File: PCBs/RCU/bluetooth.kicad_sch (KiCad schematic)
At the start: 31 parts, among them J400 USB_C_Receptacle_USB2.0, Q400 Q_NMOS_DGS, Q401 Q_NMOS_DGS, Q402 Q_PMOS_DGS, Q403 Q_NMOS_DGS, SW400 SW_Push, U400 CH340C, U401 DG2788ADN-T1-GE4, U402 ESP32-MINI-1

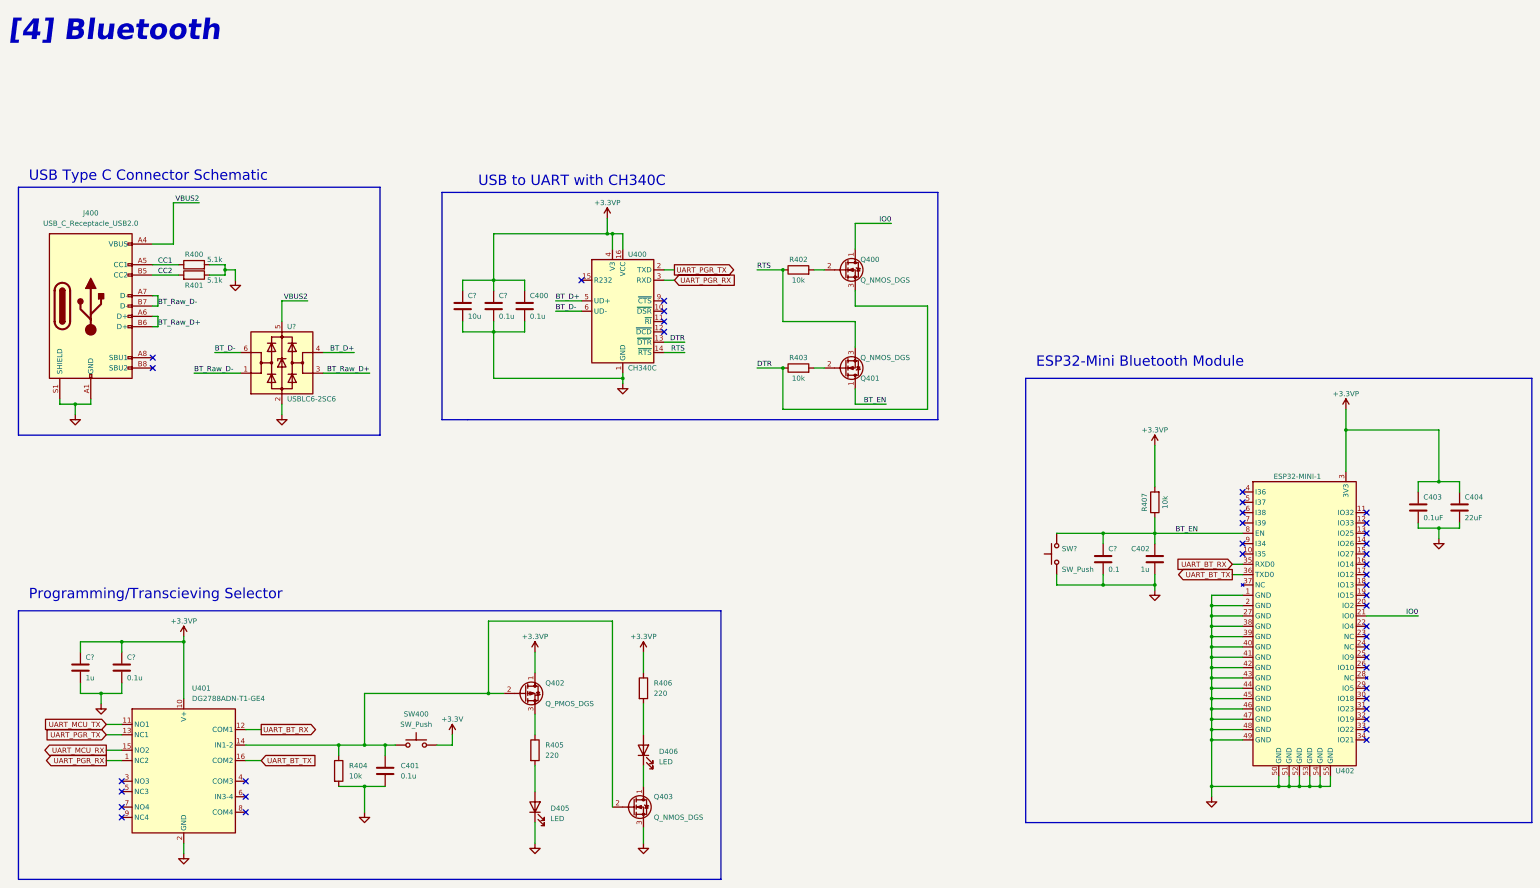
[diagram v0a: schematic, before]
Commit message: Fully annotated Bluetooth schematic
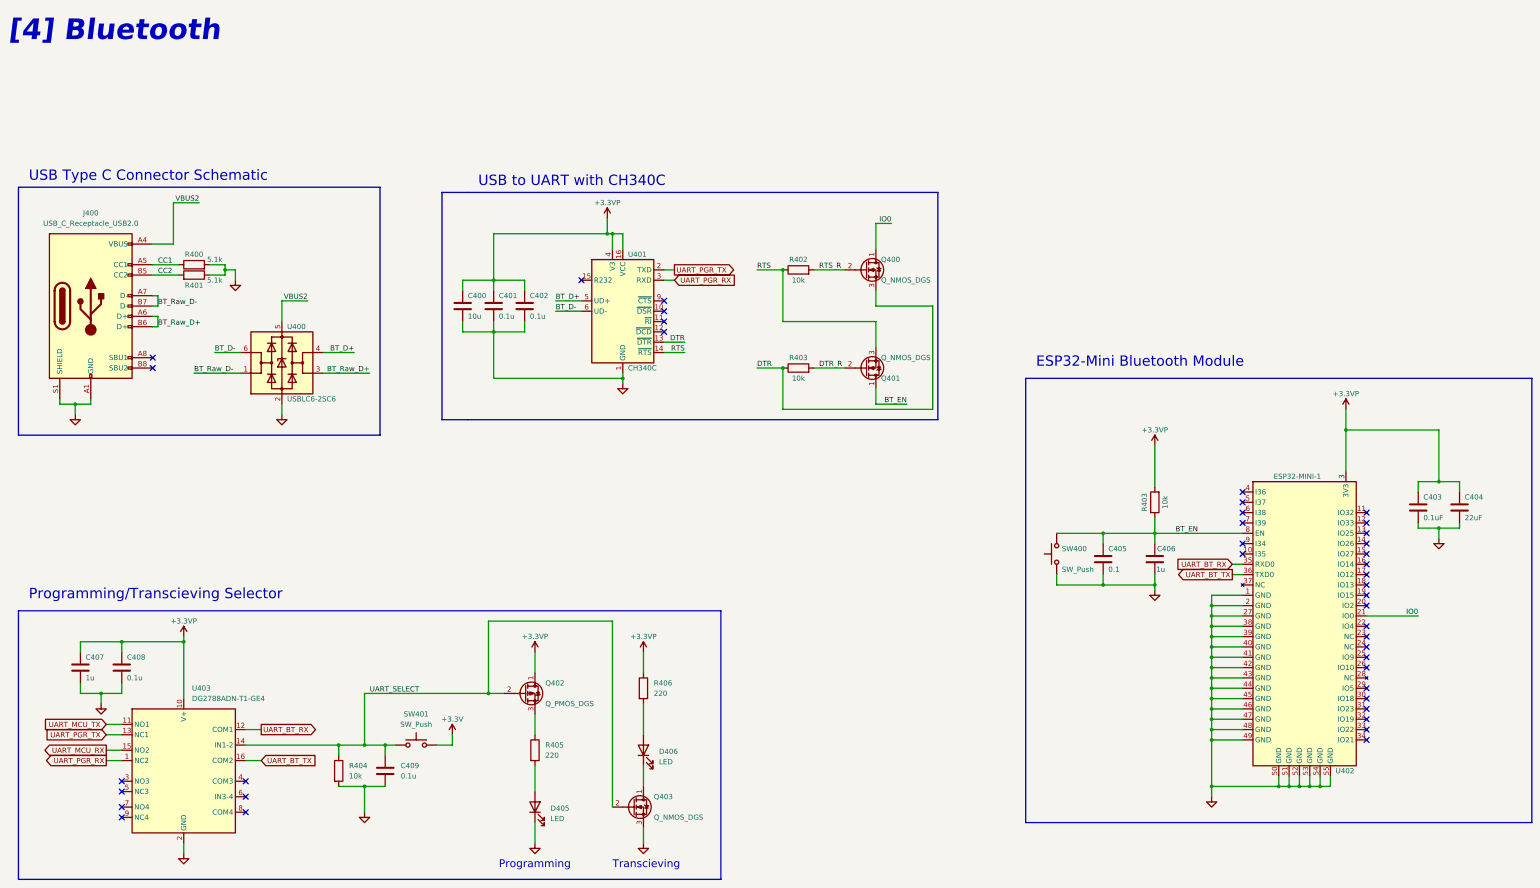
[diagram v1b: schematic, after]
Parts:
- gave numbers to parts that had none: 7
- renumbered C400 to C402, C402 to C406, C401 to C409, R407 to R403, SW400 to SW401, U400 to U401, U401 to U403
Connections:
- net UART_SELECT: now reaches C409.1, Q402.2 (G), Q403.2 (G), R404.1, SW401.1, U403.14 (IN1-2)
- net DTR_R: now reaches Q401.2 (G), R403.2
- net RTS_R: now reaches Q400.2 (G), R402.2
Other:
- note added: "Programming"
- note added: "Transcieving"
- moved on the sheet: Q400, Q401

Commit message: Schematic cleanup
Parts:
- C400: value 10u -> (none)
- C401, C402, C409: value 0.1u -> (none)
- C405: value 0.1 -> (none)
- C406: value 1u -> (none)
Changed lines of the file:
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@@
       (effects (font (size 1.27 1.27)) (justify left))
     )
-    (property "Value" "0.1u" (id 1) (at 160.02 100.33 0)
+    (property "Value" "" (id 1) (at 160.02 100.33 0)
       (effects (font (size 1.27 1.27)) (justify left))
     )
@@
       (effects (font (size 1.27 1.27)) (justify left))
     )
-    (property "Value" "0.1u" (id 1) (at 128.27 213.3599 0)
+    (property "Value" "" (id 1) (at 128.27 213.3599 0)
       (effects (font (size 1.27 1.27)) (justify left))
     )
@@
       (effects (font (size 1.27 1.27)) (justify left))
     )
-    (property "Value" "0.1u" (id 1) (at 152.4 100.33 0)
+    (property "Value" "" (id 1) (at 152.4 100.33 0)
       (effects (font (size 1.27 1.27)) (justify left))
     )
@@
       (effects (font (size 1.27 1.27)) (justify left))
     )
-    (property "Value" "10u" (id 1) (at 144.78 100.33 0)
+    (property "Value" "" (id 1) (at 144.78 100.33 0)
       (effects (font (size 1.27 1.27)) (justify left))
     )
@@
       (effects (font (size 1.27 1.27)) (justify left))
     )
-    (property "Value" "1u" (id 1) (at 316.23 162.56 0)
+    (property "Value" "" (id 1) (at 317.5 162.56 0)
       (effects (font (size 1.27 1.27)) (justify left))
     )
@@
       (effects (font (size 1.27 1.27)) (justify left))
     )
-    (property "Value" "0.1" (id 1) (at 302.26 162.56 0)
-      (effects (font (size 1.27 1.27)) (justify left))
-    )
+    (property "Value" "" (id 1) (at 302.26 162.56 0)
+      (effects (font (size 1.27 1.27)) (justify left))
+    )

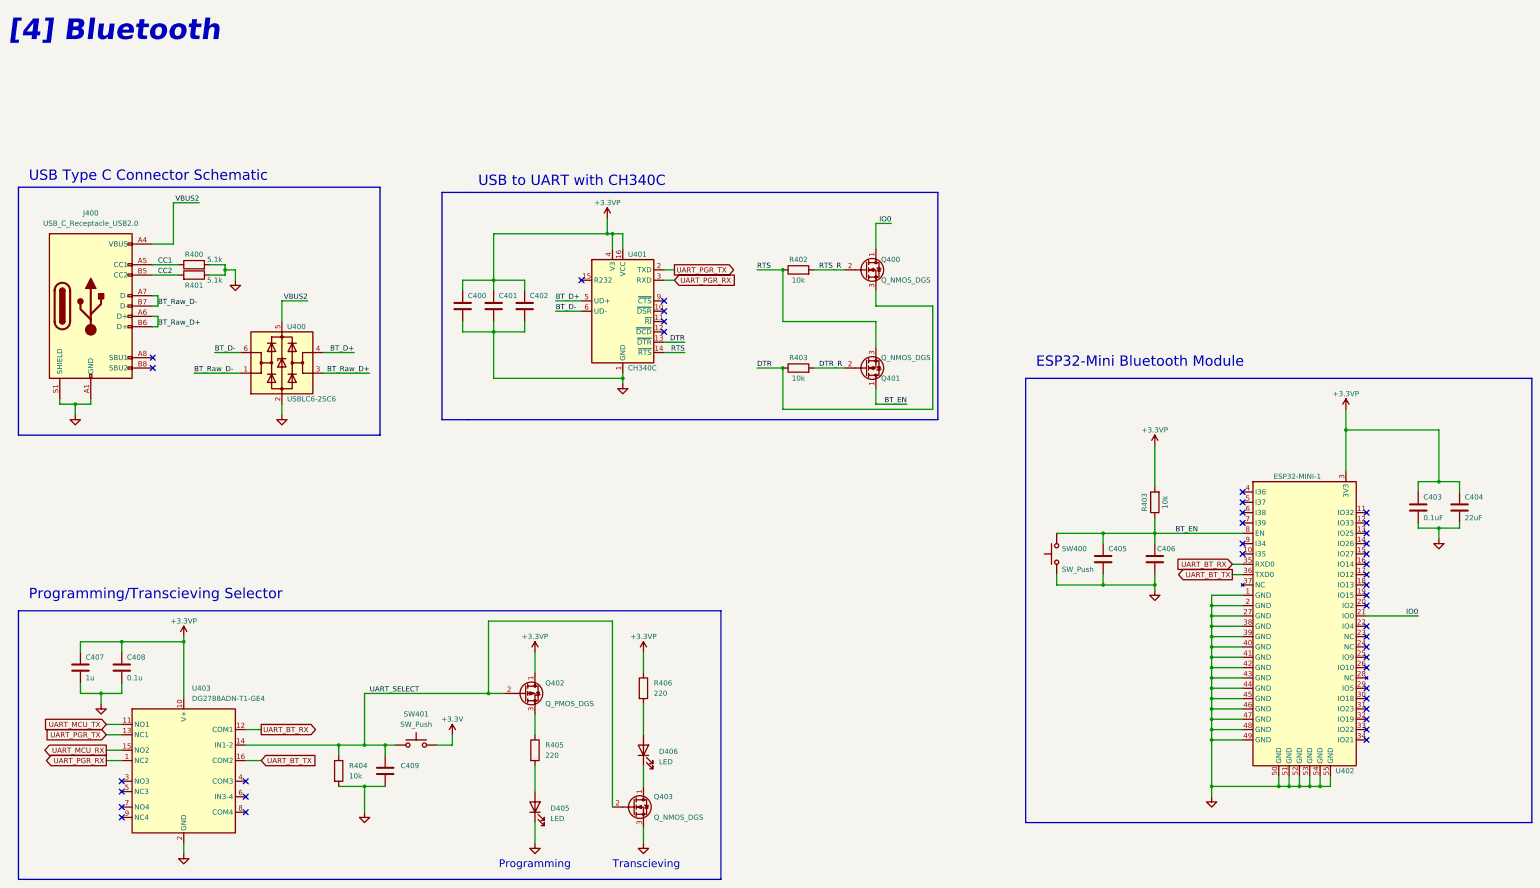
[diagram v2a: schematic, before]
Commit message: Wrote that first regulator in power schematic also powers the external memory
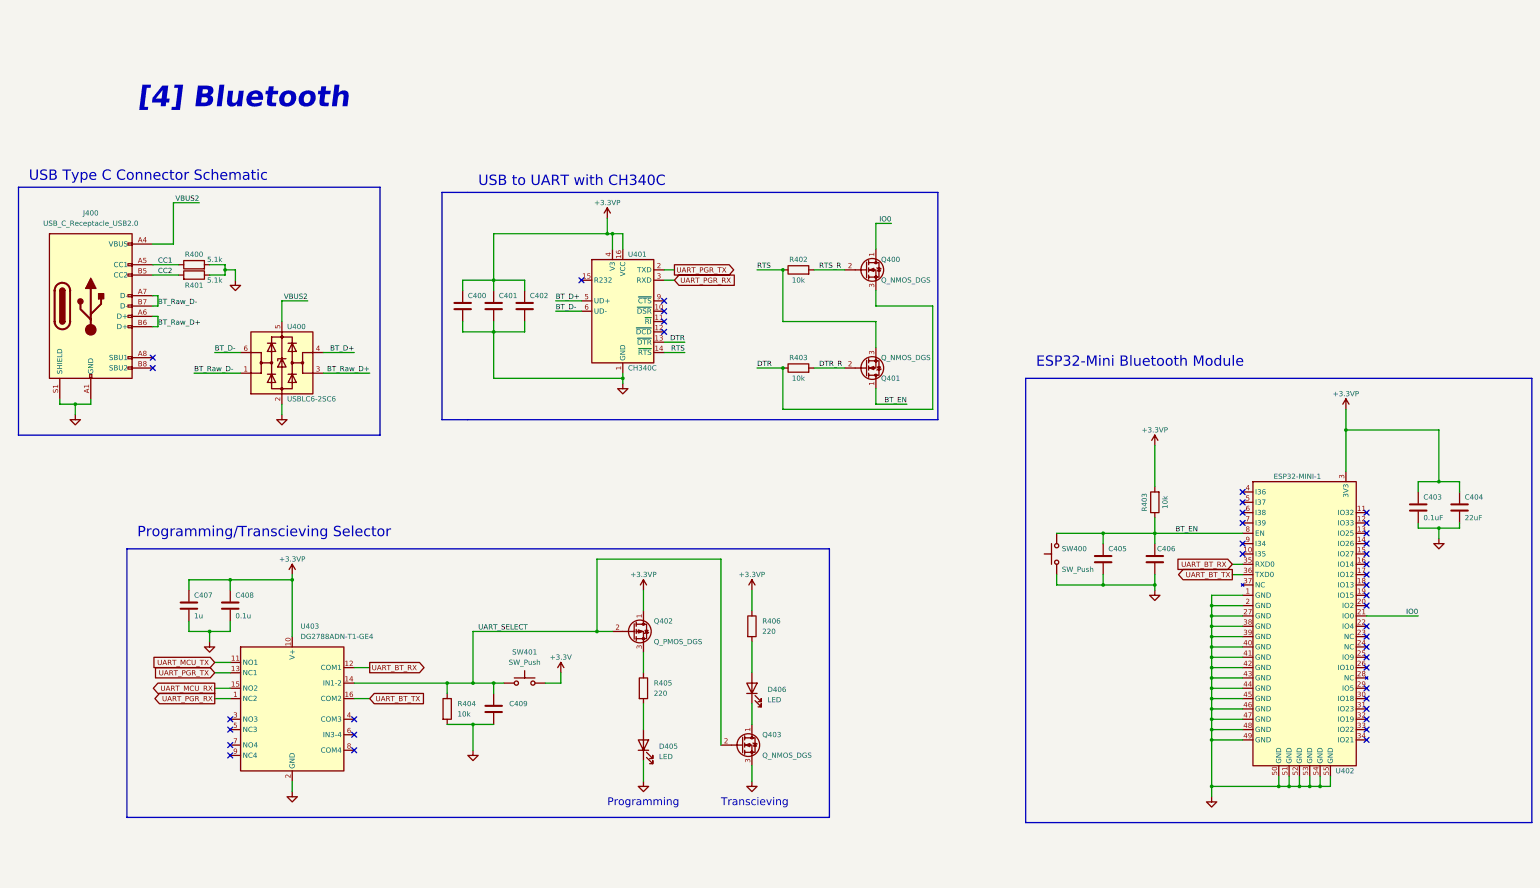
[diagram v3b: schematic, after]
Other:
- moved on the sheet: C407, C408, C409, D405, D406, Q402, Q403, R404, R405, R406, SW401, U403

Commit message: Corrected SPI_MOSI and SPI_MISO labels on U700 - external memory
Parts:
- C400: value (none) -> 10uF
- C401, C402, C405, C409: value (none) -> 0.1uF
- C406: value (none) -> 1uF
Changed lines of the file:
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@@
       (effects (font (size 1.27 1.27)) (justify left))
     )
-    (property "Value" "" (id 1) (at 160.02 100.33 0)
+    (property "Value" "0.1uF" (id 1) (at 160.02 100.33 0)
       (effects (font (size 1.27 1.27)) (justify left))
     )
@@
       (effects (font (size 1.27 1.27)) (justify left))
     )
-    (property "Value" "" (id 1) (at 154.94 198.1199 0)
+    (property "Value" "0.1uF" (id 1) (at 154.94 198.1199 0)
       (effects (font (size 1.27 1.27)) (justify left))
     )
@@
       (effects (font (size 1.27 1.27)) (justify left))
     )
-    (property "Value" "" (id 1) (at 152.4 100.33 0)
+    (property "Value" "0.1uF" (id 1) (at 152.4 100.33 0)
       (effects (font (size 1.27 1.27)) (justify left))
     )
@@
       (effects (font (size 1.27 1.27)) (justify left))
     )
-    (property "Value" "" (id 1) (at 144.78 100.33 0)
+    (property "Value" "10uF" (id 1) (at 144.78 100.33 0)
       (effects (font (size 1.27 1.27)) (justify left))
     )
@@
       (effects (font (size 1.27 1.27)) (justify left))
     )
-    (property "Value" "" (id 1) (at 317.5 162.56 0)
+    (property "Value" "1uF" (id 1) (at 317.5 162.56 0)
       (effects (font (size 1.27 1.27)) (justify left))
     )
@@
       (effects (font (size 1.27 1.27)) (justify left))
     )
-    (property "Value" "" (id 1) (at 302.26 162.56 0)
-      (effects (font (size 1.27 1.27)) (justify left))
-    )
+    (property "Value" "0.1uF" (id 1) (at 302.26 162.56 0)
+      (effects (font (size 1.27 1.27)) (justify left))
+    )

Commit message: Changed UART selector led resistor values, and assigned colours
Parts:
- D405, D406: value LED -> (none)
- R405, R406: value 220 -> (none)
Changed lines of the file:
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@@
     (effects (font (size 5.08 5.08) (thickness 1.016) bold italic) (justify left bottom))
   )
-  (text "Programming" (at 179.07 220.98 0)
+  (text "Programming" (at 205.74 220.98 0)
     (effects (font (size 1.905 1.905)) (justify left bottom))
   )
@@
     (effects (font (size 2.54 2.54)) (justify left bottom))
   )
-  (text "Transcieving\n" (at 207.01 220.98 0)
+  (text "Transcieving\n" (at 180.34 220.98 0)
     (effects (font (size 1.905 1.905)) (justify left bottom))
   )
@@
       (effects (font (size 1.27 1.27)) (justify left))
     )
-    (property "Value" "220" (id 1) (at 190.5 193.0399 0)
+    (property "Value" "" (id 1) (at 190.5 193.0399 0)
       (effects (font (size 1.27 1.27)) (justify left))
     )
@@
       (effects (font (size 1.27 1.27)) (justify right))
     )
-    (property "Value" "LED" (id 1) (at 218.44 194.6274 90)
+    (property "Value" "" (id 1) (at 218.44 194.6274 90)
       (effects (font (size 1.27 1.27)) (justify right))
     )
@@
       (effects (font (size 1.27 1.27)) (justify left))
     )
-    (property "Value" "220" (id 1) (at 217.17 177.7999 0)
+    (property "Value" "" (id 1) (at 217.17 177.7999 0)
       (effects (font (size 1.27 1.27)) (justify left))
     )
@@
       (effects (font (size 1.27 1.27)) (justify right))
     )
-    (property "Value" "LED" (id 1) (at 191.77 208.5974 90)
+    (property "Value" "" (id 1) (at 191.77 208.5974 90)
       (effects (font (size 1.27 1.27)) (justify right))
     )

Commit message: Add microcontroller, USB receptable and Connx05 footprints
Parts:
- D405: value (none) -> Green LED
- D406: value (none) -> Yellow LED
- R405: value (none) -> 40R
- R406: value (none) -> 280
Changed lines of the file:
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@@
       (effects (font (size 1.27 1.27)) (justify left))
     )
-    (property "Value" "" (id 1) (at 190.5 193.0399 0)
+    (property "Value" "40R" (id 1) (at 190.5 193.0399 0)
       (effects (font (size 1.27 1.27)) (justify left))
     )
@@
       (effects (font (size 1.27 1.27)) (justify right))
     )
-    (property "Value" "" (id 1) (at 218.44 194.6274 90)
+    (property "Value" "Yellow LED" (id 1) (at 218.44 194.6274 90)
       (effects (font (size 1.27 1.27)) (justify right))
     )
@@
       (effects (font (size 1.27 1.27)) (justify left))
     )
-    (property "Value" "" (id 1) (at 217.17 177.7999 0)
+    (property "Value" "280" (id 1) (at 217.17 177.7999 0)
       (effects (font (size 1.27 1.27)) (justify left))
     )
@@
       (effects (font (size 1.27 1.27)) (justify right))
     )
-    (property "Value" "" (id 1) (at 191.77 208.5974 90)
+    (property "Value" "Green LED" (id 1) (at 191.77 208.5974 90)
       (effects (font (size 1.27 1.27)) (justify right))
     )

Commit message: Add footprint to rest of IC's except ESP32
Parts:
- J400: footprint (none) -> Connector_USB:USB_C_Receptacle_HRO_TYPE-C-31-M-12
- U401: footprint Package_SO:SOIC-16_3.9x9.9mm_P1.27mm -> Package_SO:SOP-16_3.9x9.9mm_P1.27mm
- U403: footprint (none) -> UQFN-16(1.8x2.6):QFN40P260X180X55-16N
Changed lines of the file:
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@@
       (effects (font (size 1.27 1.27)) (justify left))
     )
-    (property "Footprint" "" (id 2) (at 82.55 175.26 0)
+    (property "Footprint" "UQFN-16(1.8x2.6):QFN40P260X180X55-16N" (id 2) (at 82.55 175.26 0)
       (effects (font (size 1.27 1.27)) hide)
     )
@@
     (property "Reference" "J400" (id 0) (at 52.07 74.93 0))
     (property "Value" "USB_C_Receptacle_USB2.0" (id 1) (at 52.07 77.47 0))
-    (property "Footprint" "" (id 2) (at 55.88 97.79 0)
+    (property "Footprint" "Connector_USB:USB_C_Receptacle_HRO_TYPE-C-31-M-12" (id 2) (at 55.88 97.79 0)
       (effects (font (size 1.27 1.27)) hide)
     )
@@
       (effects (font (size 1.27 1.27)) (justify left))
     )
-    (property "Footprint" "Package_SO:SOIC-16_3.9x9.9mm_P1.27mm" (id 2) (at 184.15 113.03 0)
+    (property "Footprint" "Package_SO:SOP-16_3.9x9.9mm_P1.27mm" (id 2) (at 184.15 113.03 0)
       (effects (font (size 1.27 1.27)) (justify left) hide)
     )

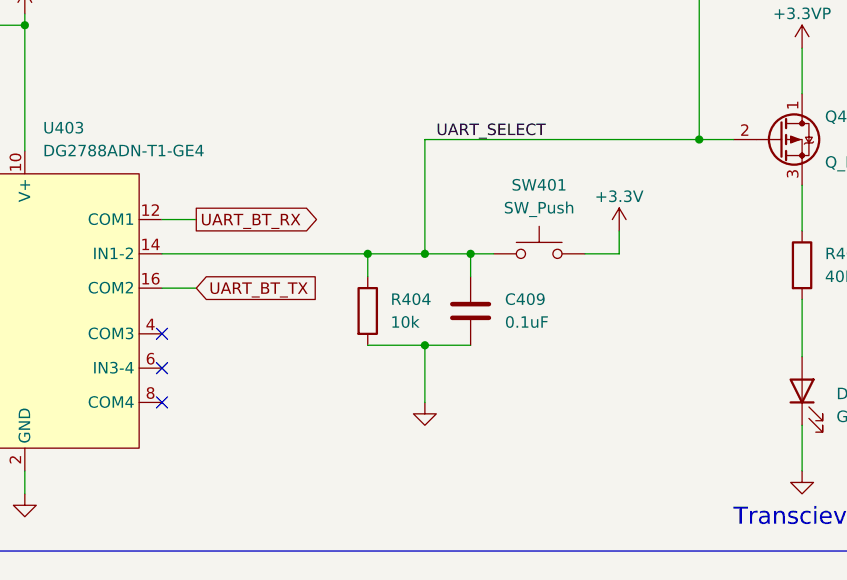
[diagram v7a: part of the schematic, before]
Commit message: Changed Programming/Transcieving button to a slide switch
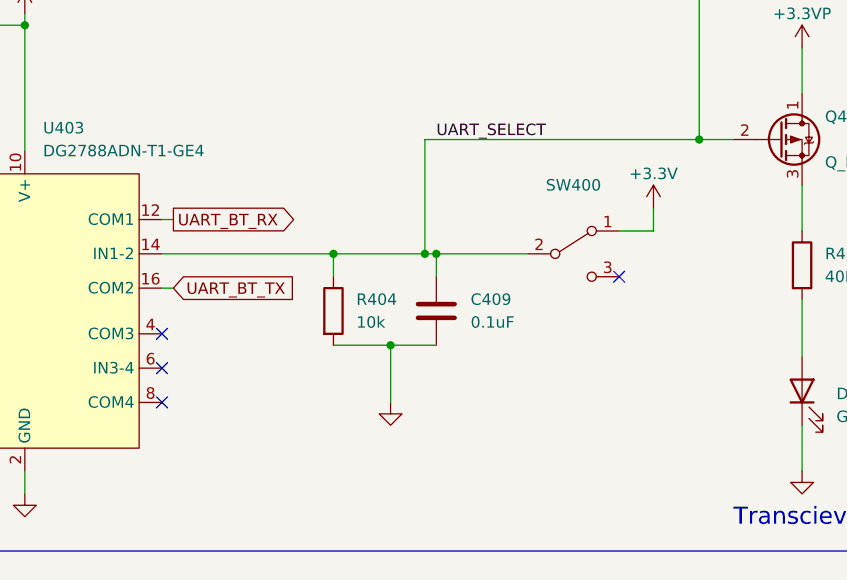
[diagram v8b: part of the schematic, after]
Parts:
- removed SW401: SW_Push, symbol Switch:SW_Push
- added SW400: (no value), symbol Switch:SW_SPDT
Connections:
- net +3V3: now also SW400.1 (A)
- net UART_SELECT: now also SW400.2 (B)
- no-connect marks 41 -> 42
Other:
- moved on the sheet: C409, R404
